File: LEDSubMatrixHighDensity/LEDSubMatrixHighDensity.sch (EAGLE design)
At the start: 129 parts, among them IC1 TLC5955DCAR, IC2 TLC5955DCAR, IC3 TLC5955DCAR, IC4 TLC5955DCAR, IC5 TLC5955DCAR, IC6 TLC5955DCAR, IC7 TLC5955DCAR, IC8 TLC5955DCAR

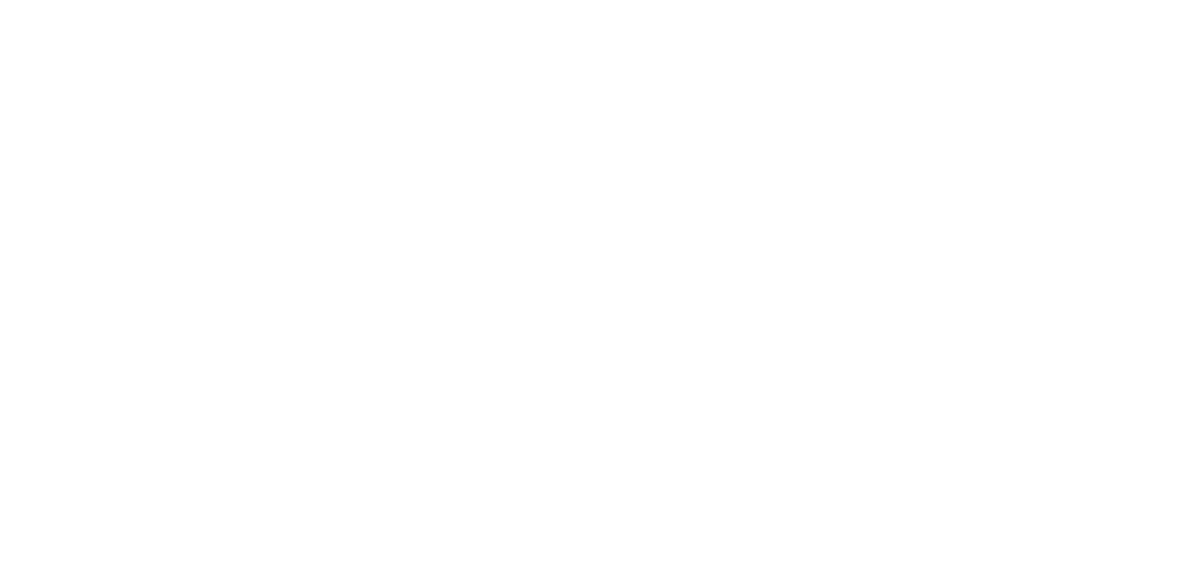
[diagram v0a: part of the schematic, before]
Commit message: Finished routing traces on high density matrix PCB
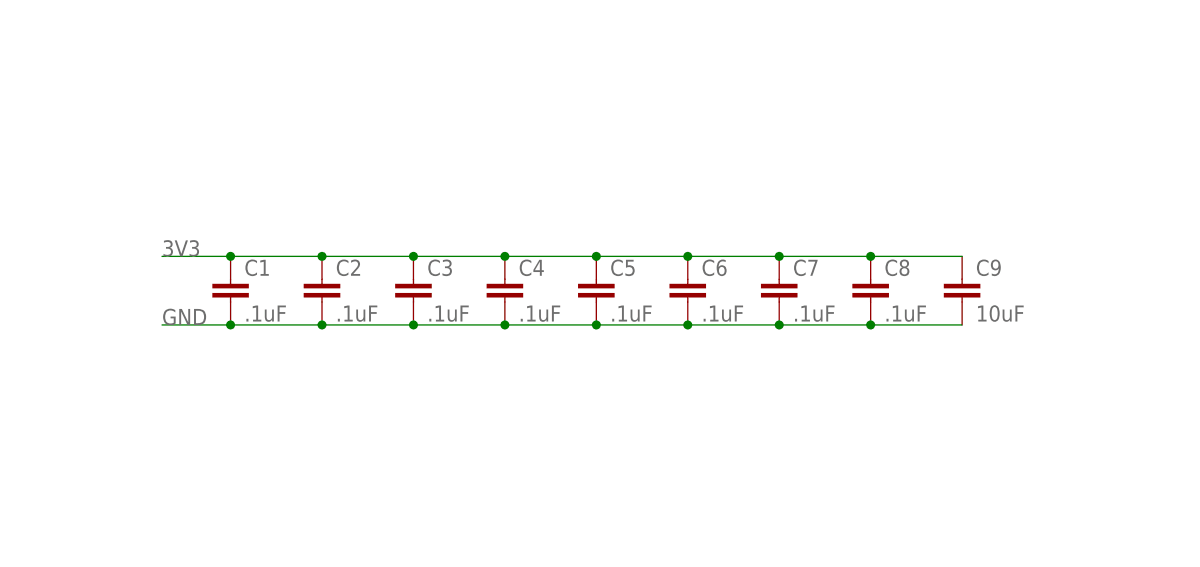
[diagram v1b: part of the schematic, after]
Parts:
- added C1, C2, C3, C4, C5, C6, C7, C8: .1uF, rcl:C-EUC0603
- added C9: 10uF, rcl:C-EUC0805
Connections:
- net 3V3: now also C1.1, C2.1, C3.1, C4.1, C5.1, C6.1, C7.1, C8.1, C9.1
- net GND: now also C1.2, C2.2, C3.2, C4.2, C5.2, C6.2, C7.2, C8.2, C9.2
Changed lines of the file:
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@@
 <part name="IC8" library="TLC5955DCAR" deviceset="TLC5955DCAR" device=""/>
 <part name="SV1" library="con-lstb" library_urn="urn:adsk.eagle:library:162" deviceset="MA06-2" device="" package3d_urn="urn:adsk.eagle:package:8342/1"/>
+<part name="C2" library="rcl" library_urn="urn:adsk.eagle:library:334" deviceset="C-EU" device="C0603" package3d_urn="urn:adsk.eagle:package:23616/2" value=".1uF"/>
+<part name="C3" library="rcl" library_urn="urn:adsk.eagle:library:334" deviceset="C-EU" device="C0603" package3d_urn="urn:adsk.eagle:package:23616/2" value=".1uF"/>
+<part name="C4" library="rcl" library_urn="urn:adsk.eagle:library:334" deviceset="C-EU" device="C0603" package3d_urn="urn:adsk.eagle:package:23616/2" value=".1uF"/>
+<part name="C5" library="rcl" library_urn="urn:adsk.eagle:library:334" deviceset="C-EU" device="C0603" package3d_urn="urn:adsk.eagle:package:23616/2" value=".1uF"/>
+<part name="C6" library="rcl" library_urn="urn:adsk.eagle:library:334" deviceset="C-EU" device="C0603" package3d_urn="urn:adsk.eagle:package:23616/2" value=".1uF"/>
+<part name="C7" library="rcl" library_urn="urn:adsk.eagle:library:334" deviceset="C-EU" device="C0603" package3d_urn="urn:adsk.eagle:package:23616/2" value=".1uF"/>
+<part name="C8" library="rcl" library_urn="urn:adsk.eagle:library:334" deviceset="C-EU" device="C0603" package3d_urn="urn:adsk.eagle:package:23616/2" value=".1uF"/>
+<part name="C9" library="rcl" library_urn="urn:adsk.eagle:library:334" deviceset="C-EU" device="C0805" package3d_urn="urn:adsk.eagle:package:23617/2" value="10uF"/>
+<part name="C1" library="rcl" library_urn="urn:adsk.eagle:library:334" deviceset="C-EU" device="C0603" package3d_urn="urn:adsk.eagle:package:23616/2" value=".1uF"/>
 </parts>
 <sheets>
@@
 <attribute name="NAME" x="-46.99" y="-414.782" size="1.778" layer="95" rot="R180"/>
 </instance>
+<instance part="C2" gate="G$1" x="27.94" y="-403.86" smashed="yes">
+<attribute name="NAME" x="29.464" y="-403.479" size="1.778" layer="95"/>
+<attribute name="VALUE" x="29.464" y="-408.559" size="1.778" layer="96"/>
+</instance>
+<instance part="C3" gate="G$1" x="38.1" y="-403.86" smashed="yes">
+<attribute name="NAME" x="39.624" y="-403.479" size="1.778" layer="95"/>
+<attribute name="VALUE" x="39.624" y="-408.559" size="1.778" layer="96"/>
+</instance>
+<instance part="C4" gate="G$1" x="48.26" y="-403.86" smashed="yes">
+<attribute name="NAME" x="49.784" y="-403.479" size="1.778" layer="95"/>
+<attribute name="VALUE" x="49.784" y="-408.559" size="1.778" layer="96"/>
+</instance>
+<instance part="C5" gate="G$1" x="58.42" y="-403.86" smashed="yes">
+<attribute name="NAME" x="59.944" y="-403.479" size="1.778" layer="95"/>
+<attribute name="VALUE" x="59.944" y="-408.559" size="1.778" layer="96"/>
+</instance>
+<instance part="C6" gate="G$1" x="68.58" y="-403.86" smashed="yes">
+<attribute name="NAME" x="70.104" y="-403.479" size="1.778" layer="95"/>
+<attribute name="VALUE" x="70.104" y="-408.559" size="1.778" layer="96"/>
+</instance>
+<instance part="C7" gate="G$1" x="78.74" y="-403.86" smashed="yes">
+<attribute name="NAME" x="80.264" y="-403.479" size="1.778" layer="95"/>
+<attribute name="VALUE" x="80.264" y="-408.559" size="1.778" layer="96"/>
+</instance>
+<instance part="C8" gate="G$1" x="88.9" y="-403.86" smashed="yes">
+<attribute name="NAME" x="90.424" y="-403.479" size="1.778" layer="95"/>
+<attribute name="VALUE" x="90.424" y="-408.559" size="1.778" layer="96"/>
+</instance>
+<instance part="C9" gate="G$1" x="99.06" y="-403.86" smashed="yes">
+<attribute name="NAME" x="100.584" y="-403.479" size="1.778" layer="95"/>
+<attribute name="VALUE" x="100.584" y="-408.559" size="1.778" layer="96"/>
+</instance>
+<instance part="C1" gate="G$1" x="17.78" y="-403.86" smashed="yes">
+<attribute name="NAME" x="19.304" y="-403.479" size="1.778" layer="95"/>
+<attribute name="VALUE" x="19.304" y="-408.559" size="1.778" layer="96"/>
+</instance>
 </instances>
 <busses>
@@
 <label x="-33.02" y="-408.94" size="1.778" layer="95" rot="MR0"/>
 </segment>
+<segment>
+<pinref part="C1" gate="G$1" pin="1"/>
+<pinref part="C2" gate="G$1" pin="1"/>
+<wire x1="17.78" y1="-401.32" x2="27.94" y2="-401.32" width="0.1524" layer="91"/>
+<pinref part="C3" gate="G$1" pin="1"/>
+<wire x1="27.94" y1="-401.32" x2="38.1" y2="-401.32" width="0.1524" layer="91"/>
+<junction x="27.94" y="-401.32"/>
+<pinref part="C4" gate="G$1" pin="1"/>
+<wire x1="38.1" y1="-401.32" x2="48.26" y2="-401.32" width="0.1524" layer="91"/>
+<junction x="38.1" y="-401.32"/>
+<pinref part="C5" gate="G$1" pin="1"/>
+<wire x1="48.26" y1="-401.32" x2="58.42" y2="-401.32" width="0.1524" layer="91"/>
+<junction x="48.26" y="-401.32"/>
+<pinref part="C6" gate="G$1" pin="1"/>
+<wire x1="58.42" y1="-401.32" x2="68.58" y2="-401.32" width="0.1524" layer="91"/>
+<junction x="58.42" y="-401.32"/>
+<pinref part="C7" gate="G$1" pin="1"/>
+<wire x1="68.58" y1="-401.32" x2="78.74" y2="-401.32" width="0.1524" layer="91"/>
+<junction x="68.58" y="-401.32"/>
+<pinref part="C8" gate="G$1" pin="1"/>
+<wire x1="78.74" y1="-401.32" x2="88.9" y2="-401.32" width="0.1524" layer="91"/>
+<junction x="78.74" y="-401.32"/>
+<pinref part="C9" gate="G$1" pin="1"/>
+<wire x1="88.9" y1="-401.32" x2="99.06" y2="-401.32" width="0.1524" layer="91"/>
+<junction x="88.9" y="-401.32"/>
+<wire x1="17.78" y1="-401.32" x2="10.16" y2="-401.32" width="0.1524" layer="91"/>
+<junction x="17.78" y="-401.32"/>
+<label x="10.16" y="-401.32" size="1.778" layer="95"/>
+</segment>
 </net>
 <net name="SCLK" class="0">
@@
 <label x="-33.02" y="-411.48" size="1.778" layer="95" rot="MR0"/>
 </segment>
-</net>
+<segment>
+<pinref part="C1" gate="G$1" pin="2"/>
+<pinref part="C2" gate="G$1" pin="2"/>
+<wire x1="17.78" y1="-408.94" x2="27.94" y2="-408.94" width="0.1524" layer="91"/>
+<pinref part="C3" gate="G$1" pin="2"/>
+<wire x1="38.1" y1="-408.94" x2="27.94" y2="-408.94" width="0.1524" layer="91"/>
+<junction x="27.94" y="-408.94"/>
+<pinref part="C4" gate="G$1" pin="2"/>
+<wire x1="38.1" y1="-408.94" x2="48.26" y2="-408.94" width="0.1524" layer="91"/>
+<junction x="38.1" y="-408.94"/>
+<pinref part="C5" gate="G$1" pin="2"/>
+<wire x1="48.26" y1="-408.94" x2="58.42" y2="-408.94" width="0.1524" layer="91"/>
+<junction x="48.26" y="-408.94"/>
+<pinref part="C6" gate="G$1" pin="2"/>
+<wire x1="58.42" y1="-408.94" x2="68.58" y2="-408.94" width="0.1524" layer="91"/>
+<junction x="58.42" y="-408.94"/>
+<pinref part="C7" gate="G$1" pin="2"/>
+<wire x1="68.58" y1="-408.94" x2="78.74" y2="-408.94" width="0.1524" layer="91"/>
+<junction x="68.58" y="-408.94"/>
+<pinref part="C8" gate="G$1" pin="2"/>
+<wire x1="78.74" y1="-408.94" x2="88.9" y2="-408.94" width="0.1524" layer="91"/>
+<junction x="78.74" y="-408.94"/>
+<pinref part="C9" gate="G$1" pin="2"/>
+<wire x1="88.9" y1="-408.94" x2="99.06" y2="-408.94" width="0.1524" layer="91"/>
+<junction x="88.9" y="-408.94"/>
+<wire x1="17.78" y1="-408.94" x2="10.16" y2="-408.94" width="0.1524" layer="91"/>
+<junction x="17.78" y="-408.94"/>
+<label x="10.16" y="-408.94" size="1.778" layer="95"/>
+</segment>
+</net>

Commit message: High density PCB fixes
Fixed airwires errors and grouped components on schematic
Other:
- note removed: "ADD DECOUPLING CAPACITORS (.01uF or .1uF)"
- note removed: "ADD DECOUPLING CAPACITORS at power bridge (10uF)"
- moved on the sheet: C1, C2, C3, C4, C5, C6, C7, C8, C9, IC1, IC2, IC3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

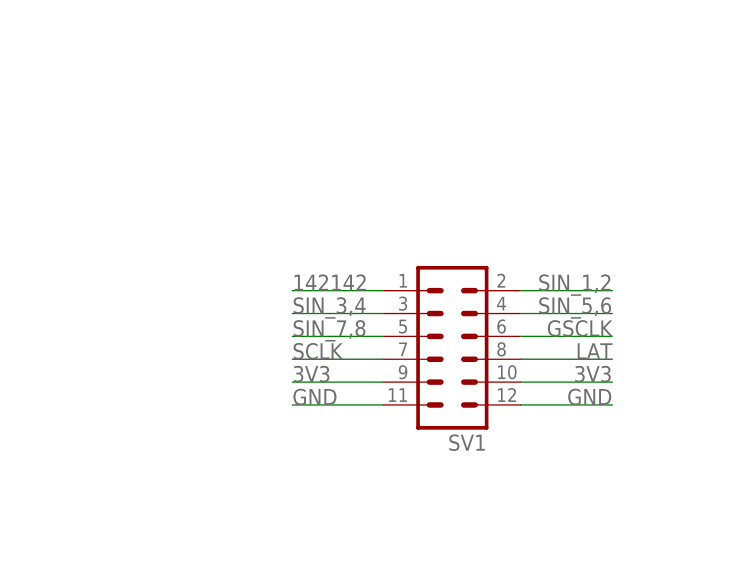
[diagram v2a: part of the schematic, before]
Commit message: Finalized LED Matrix schematic and board files
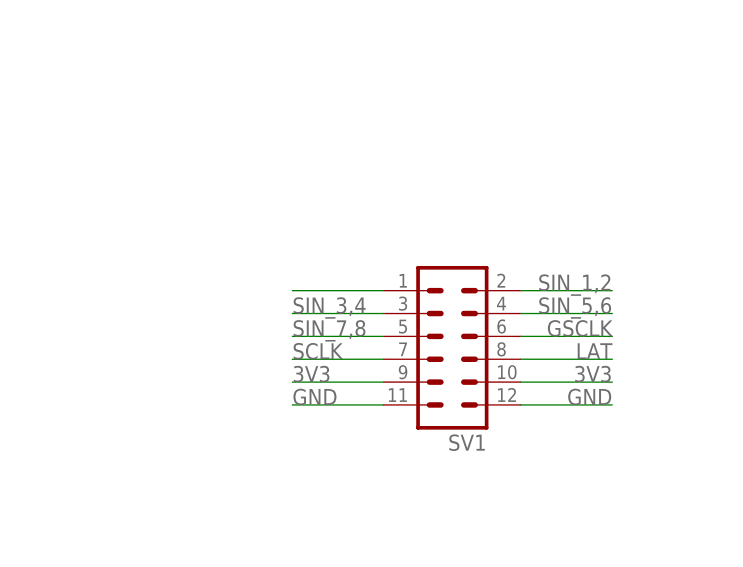
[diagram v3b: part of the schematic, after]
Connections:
- net 142142 renamed N$1
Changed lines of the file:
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@@
 </segment>
 </net>
-<net name="142142" class="0">
+<net name="N$1" class="0">
 <segment>
 <pinref part="SV1" gate="1" pin="1"/>
 <wire x1="-723.9" y1="20.32" x2="-734.06" y2="20.32" width="0.1524" layer="91"/>
-<label x="-734.06" y="20.32" size="1.778" layer="95"/>
 </segment>
 </net>
